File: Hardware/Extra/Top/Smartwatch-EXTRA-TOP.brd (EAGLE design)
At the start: 38 x 38 mm, 72 parts, among them U1 NRF52832_MODULE_MDBT42, U3 FT231XS, U4 PHOTOTRANSISTOR, U5 MCP9808-MSOP8

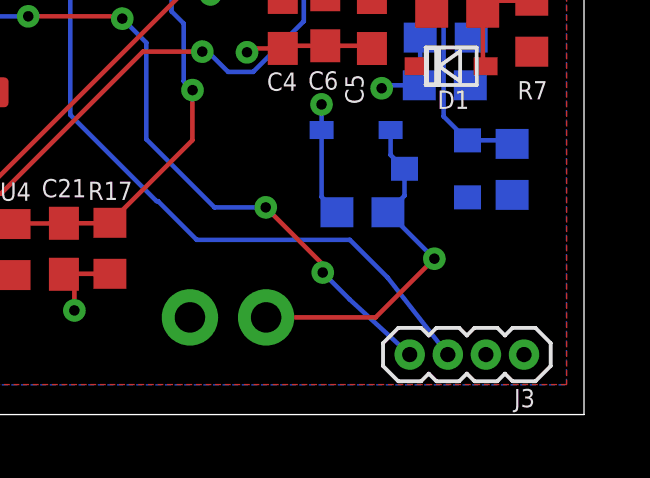
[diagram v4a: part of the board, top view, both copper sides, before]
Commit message: Encoder changed, BOMs updated
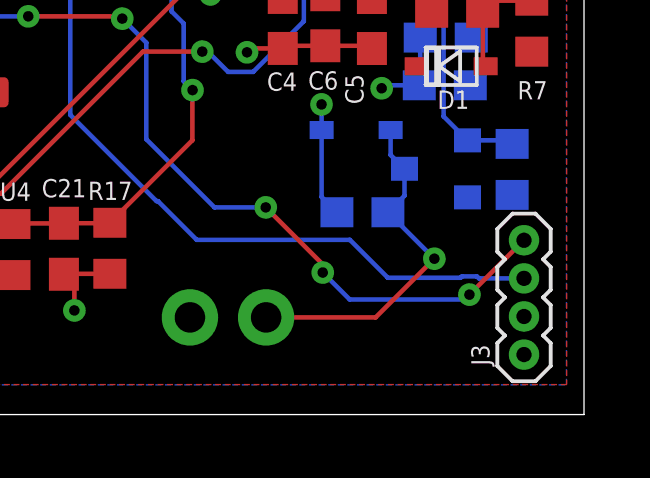
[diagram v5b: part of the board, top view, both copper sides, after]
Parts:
- C2: value 10u -> 10uF
- C21: value 2.2u -> 2.2uF
- C23: value 10p -> 10pF
- L1: value 10u -> 10uH
- turned J3 to 90 degrees
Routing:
- net SDA: track 63.8 -> 67.7 mm, vias 9 -> 10
- net SCL: track 61.5 -> 62.9 mm
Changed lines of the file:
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@@
 </layers>
 <board>
-<fusionsync huburn="a.YnVzaW5lc3M6cHVyZHVlMjIyNA" projecturn="a.YnVzaW5lc3M6cHVyZHVlMjIyNCMyMDIxMDMyNzM5NzIwMDMyNg" f3durn="urn:adsk.wipprod:dm.lineage:XFHoWaPkQBmQ3nj1vLUEBw" pcbguid="" lastpulledtime="" lastsyncedchangeguid="" latestrevisionid="3a5e7feb-a195-42dd-a08a-2611ee65cf8f" lastsyncedrevisionid="3a5e7feb-a195-42dd-a08a-2611ee65cf8f" lastboardhashguid="5192e39e-b93b-5078-4a78-5802325fcc51" lastpushedtime="2021-03-27T21:16:43Z" linktopcb3d="true"/>
+<fusionsync huburn="a.YnVzaW5lc3M6cHVyZHVlMjIyNA" projecturn="a.YnVzaW5lc3M6cHVyZHVlMjIyNCMyMDIxMDMyNzM5NzIwMDMyNg" f3durn="urn:adsk.wipprod:dm.lineage:XFHoWaPkQBmQ3nj1vLUEBw" pcbguid="" lastpulledtime="" lastsyncedchangeguid="" latestrevisionid="7c4fc147-7280-49f2-a8ff-9dc003aacbf2" lastsyncedrevisionid="7c4fc147-7280-49f2-a8ff-9dc003aacbf2" lastboardhashguid="22cbd7ec-4fab-d891-ac62-eccdf797752f" lastpushedtime="2021-03-27T21:42:09Z" linktopcb3d="true"/>
 <fusionteam huburn="a.YnVzaW5lc3M6cHVyZHVlMjIyNA" projecturn="a.YnVzaW5lc3M6cHVyZHVlMjIyNCNEMjAyMTAyMDYzODAwMDMxMjY" folderUrn="urn:adsk.wipprod:fs.folder:co.YdOB1KMQSXe9hTG6FhLD9w" urn="urn:adsk.wipprod:dm.lineage:W-tqdEdMRpy7A-WNC3jHJw"  versionUrn="urn:adsk.wipprod:fs.file:vf.W-tqdEdMRpy7A-WNC3jHJw?version=1" camFileUrn="" camFileVersionUrn="" lastpublishedchangeguid="9cd7a9d6-e81f-3132-e714-1a28a52f2c30"/>
 <plain>
@@
 <attribute name="VALUE" x="30.310865625" y="13.513784375" size="0.7112" layer="27" rot="R270"/>
 </element>
-<element name="C2" library="LinnesLab-Passives" package="C0805" override_package3d_urn="urn:adsk.eagle:package:27670968/2" override_package_urn="urn:adsk.eagle:footprint:27670970/1" value="10u" x="2.31901875" y="32.16148125" smashed="yes" rot="R90" grouprefs="MICROCONTROLLER">
+<element name="C2" library="LinnesLab-Passives" package="C0805" override_package3d_urn="urn:adsk.eagle:package:27670968/2" override_package_urn="urn:adsk.eagle:footprint:27670970/1" value="10uF" x="2.31901875" y="32.16148125" smashed="yes" rot="R90" grouprefs="MICROCONTROLLER">
 <attribute name="NAME" x="3.279140625" y="35.227259375" size="0.6096" layer="25" rot="R180"/>
 <attribute name="VALUE" x="4.22401875" y="30.89148125" size="0.7112" layer="27" rot="R90"/>
 </element>
-<element name="L1" library="LinnesLab-Passives" package="L0603" override_package3d_urn="urn:adsk.eagle:package:27669957/2" override_package_urn="urn:adsk.eagle:footprint:27669958/1" override_locally_modified="yes" value="10u" x="20.0353" y="25.997940625" smashed="yes" rot="R90" grouprefs="MICROCONTROLLER">
+<element name="L1" library="LinnesLab-Passives" package="L0603" override_package3d_urn="urn:adsk.eagle:package:27669957/2" override_package_urn="urn:adsk.eagle:footprint:27669958/1" override_locally_modified="yes" value="10uH" x="20.0353" y="25.997940625" smashed="yes" rot="R90" grouprefs="MICROCONTROLLER">
 <attribute name="NAME" x="20.907721875" y="26.149021875" size="0.6096" layer="25" rot="R270"/>
 <attribute name="VALUE" x="21.6863" y="25.362940625" size="0.7112" layer="27" rot="R90"/>
@@
 <attribute name="VALUE" x="32.697140625" y="18.93091875" size="0.7112" layer="27" rot="R270"/>
 </element>
-<element name="U1" library="LinnesLab-Microcontrollers" package="BLE_MODULE_RAYTAC_MDBT42" override_package3d_urn="urn:adsk.eagle:package:18593121/2" override_package_urn="urn:adsk.eagle:footprint:18593122/1" override_locally_modified="yes" value="NRF52832_MODULE_MDBT42" x="27.406" y="29.597" smashed="yes" grouprefs="MICROCONTROLLER">
+<element name="U1" library="LinnesLab-Microcontrollers" package="BLE_MODULE_RAYTAC_MDBT42" override_package3d_urn="urn:adsk.eagle:package:27726002/2" override_package_urn="urn:adsk.eagle:footprint:27726003/1" override_locally_modified="yes" value="NRF52832_MODULE_MDBT42" x="27.406" y="29.597" smashed="yes" grouprefs="MICROCONTROLLER">
 <attribute name="NAME" x="20.76961875" y="34.8617625" size="0.6096" layer="25" ratio="18"/>
 <attribute name="SPICEPREFIX" value="X" x="27.406" y="29.597" size="1.778" layer="27" display="off"/>
@@
 <attribute name="VALUE" x="24.100459375" y="4.906640625" size="1.27" layer="27" rot="R90"/>
 </element>
-<element name="C21" library="LinnesLab-Passives" package="C0603" override_package3d_urn="urn:adsk.eagle:package:27669811/2" override_package_urn="urn:adsk.eagle:footprint:27669812/1" value="2.2u" x="20.6638375" y="5.526403125" smashed="yes" rot="R270">
+<element name="C21" library="LinnesLab-Passives" package="C0603" override_package3d_urn="urn:adsk.eagle:package:27669811/2" override_package_urn="urn:adsk.eagle:footprint:27669812/1" value="2.2uF" x="20.6638375" y="5.526403125" smashed="yes" rot="R270">
 <attribute name="NAME" x="21.40648125" y="7.850203125" size="0.6096" layer="25" rot="R180"/>
 <attribute name="VALUE" x="18.7588375" y="6.161403125" size="1.27" layer="27" rot="R270"/>
 </element>
-<element name="J3" library="LinnesLab-Connectors" package="1X04_1.27MM" override_package3d_urn="urn:adsk.eagle:package:27725590/2" override_package_urn="urn:adsk.eagle:footprint:27725591/1" value="" x="36" y="2" smashed="yes" rot="R180">
-<attribute name="NAME" x="36.365759375" y="0.851921875" size="0.6096" layer="25" font="vector" ratio="20" rot="R180"/>
-<attribute name="VALUE" x="36.381" y="3.651" size="0.6096" layer="27" font="vector" ratio="20" rot="R180"/>
+<element name="J3" library="LinnesLab-Connectors" package="1X04_1.27MM" override_package3d_urn="urn:adsk.eagle:package:27725590/2" override_package_urn="urn:adsk.eagle:footprint:27725591/1" value="" x="36" y="2" smashed="yes" rot="R90">
+<attribute name="NAME" x="34.851921875" y="1.634240625" size="0.6096" layer="25" font="vector" ratio="20" rot="R90"/>
+<attribute name="VALUE" x="37.651" y="1.619" size="0.6096" layer="27" font="vector" ratio="20" rot="R90"/>
 </element>
 <element name="C22" library="LinnesLab-Passives" package="C0603" override_package3d_urn="urn:adsk.eagle:package:27669815/2" override_package_urn="urn:adsk.eagle:footprint:27669816/1" value="100n" x="13.0403875" y="26.00068125" smashed="yes" rot="R90">
@@
 <attribute name="VALUE" x="31.673959375" y="7.8189875" size="0.635" layer="28" rot="MR0"/>
 </element>
-<element name="C23" library="LinnesLab-Passives" package="C0603" override_package3d_urn="urn:adsk.eagle:package:27669817/2" override_package_urn="urn:adsk.eagle:footprint:27669818/1" value="10p" x="30.614775" y="6.743328125" smashed="yes" rot="MR0">
+<element name="C23" library="LinnesLab-Passives" package="C0603" override_package3d_urn="urn:adsk.eagle:package:27669817/2" override_package_urn="urn:adsk.eagle:footprint:27669818/1" value="10pF" x="30.614775" y="6.743328125" smashed="yes" rot="MR0">
 <attribute name="NAME" x="31.033875" y="7.58406875" size="0.6096" layer="26" rot="MR0"/>
 <attribute name="VALUE" x="31.249775" y="4.838328125" size="1.27" layer="28" rot="MR0"/>
@@
 <attribute name="VALUE" x="32.755684375" y="14.470746875" size="1.27" layer="28" rot="MR180"/>
 </element>
-<element name="J4" library="LinnesLab-Connectors" package="1X03_1.27MM" override_package3d_urn="urn:adsk.eagle:package:27725632/2" override_package_urn="urn:adsk.eagle:footprint:27725633/1" value="" x="13.89" y="33" smashed="yes">
+<element name="J4" library="LinnesLab-Connectors" package="1X03_1.27MM" override_package3d_urn="urn:adsk.eagle:package:27725632/3" override_package_urn="urn:adsk.eagle:footprint:27725633/1" value="" x="13.89" y="33" smashed="yes">
 <attribute name="NAME" x="13.509" y="34.016" size="0.6096" layer="25" font="vector" ratio="20"/>
 <attribute name="VALUE" x="13.509" y="31.349" size="0.6096" layer="27" font="vector" ratio="20"/>
@@
 <via x="29.29128125" y="4.734559375" extent="1-16" drill="0.35"/>
 <wire x1="29.29128125" y1="4.734559375" x2="30.19" y2="3.835840625" width="0.1524" layer="16"/>
-<wire x1="30.19" y1="3.835840625" x2="32.19" y2="2" width="0.1524" layer="16"/>
+<wire x1="30.19" y1="3.835840625" x2="34.0186625" y2="3.835840625" width="0.1524" layer="16"/>
+<wire x1="34.0186625" y1="3.835840625" x2="34.18078125" y2="3.997959375" width="0.1524" layer="16"/>
+<via x="34.18078125" y="3.997959375" extent="1-16" drill="0.35"/>
+<wire x1="34.18078125" y1="3.997959375" x2="35.992821875" y2="5.81" width="0.1524" layer="1"/>
+<wire x1="35.992821875" y1="5.81" x2="36" y2="5.81" width="0.1524" layer="1"/>
 </signal>
 <signal name="SCL">
@@
 <wire x1="25.09001875" y1="5.82421875" x2="30.195521875" y2="5.82421875" width="0.1524" layer="16"/>
 <wire x1="30.195521875" y1="5.82421875" x2="31.46" y2="4.559740625" width="0.1524" layer="16"/>
-<wire x1="31.46" y1="4.559740625" x2="33.46" y2="2" width="0.1524" layer="16"/>
 <wire x1="23.800975" y1="7.1132625" x2="25.09001875" y2="5.82421875" width="0.1524" layer="16"/>
+<wire x1="33.92943125" y1="4.6047625" x2="34.43213125" y2="4.6047625" width="0.1524" layer="16"/>
+<wire x1="34.43213125" y1="4.6047625" x2="34.49689375" y2="4.54" width="0.1524" layer="16"/>
+<wire x1="34.49689375" y1="4.54" x2="36" y2="4.54" width="0.1524" layer="16"/>
+<wire x1="31.46" y1="4.559740625" x2="33.884409375" y2="4.559740625" width="0.1524" layer="16"/>
+<wire x1="33.884409375" y1="4.559740625" x2="33.92943125" y2="4.6047625" width="0.1524" layer="16"/>
 </signal>
 <signal name="SCK">

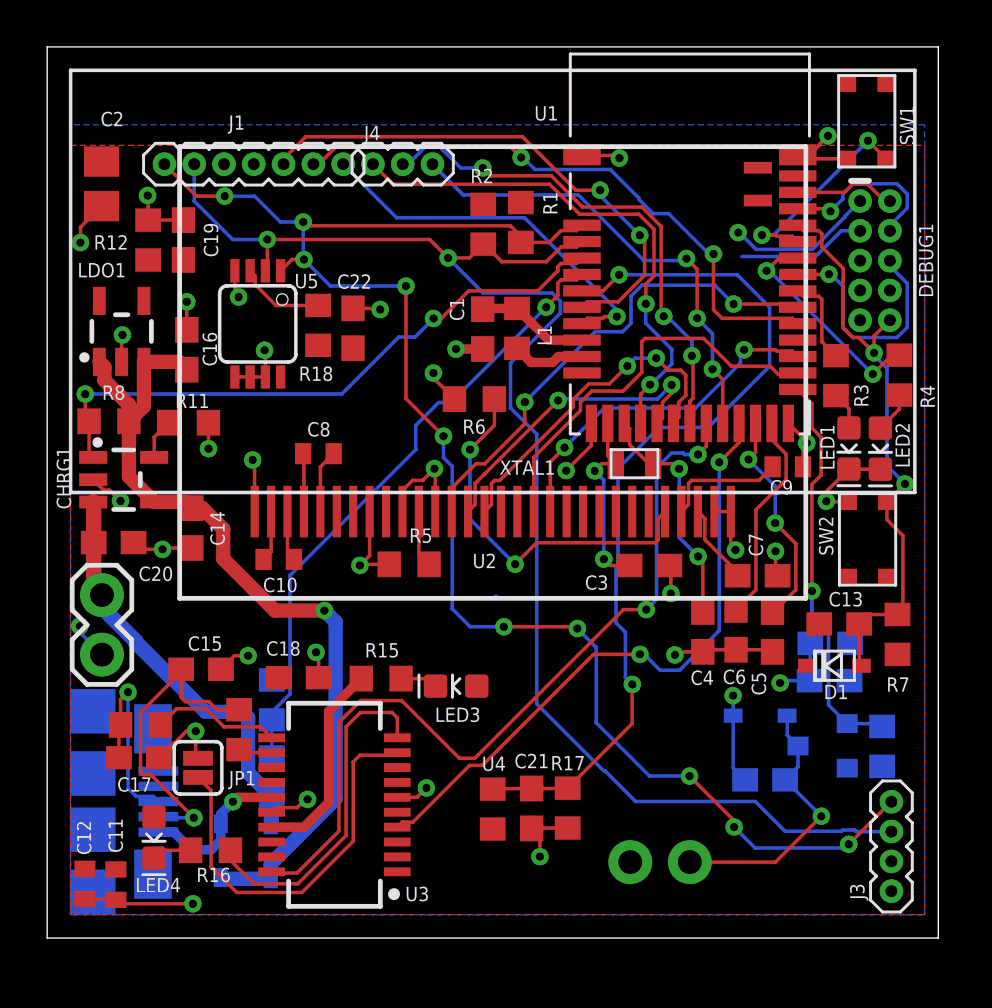
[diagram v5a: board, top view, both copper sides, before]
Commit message: Removed GPS, rearranged some other components
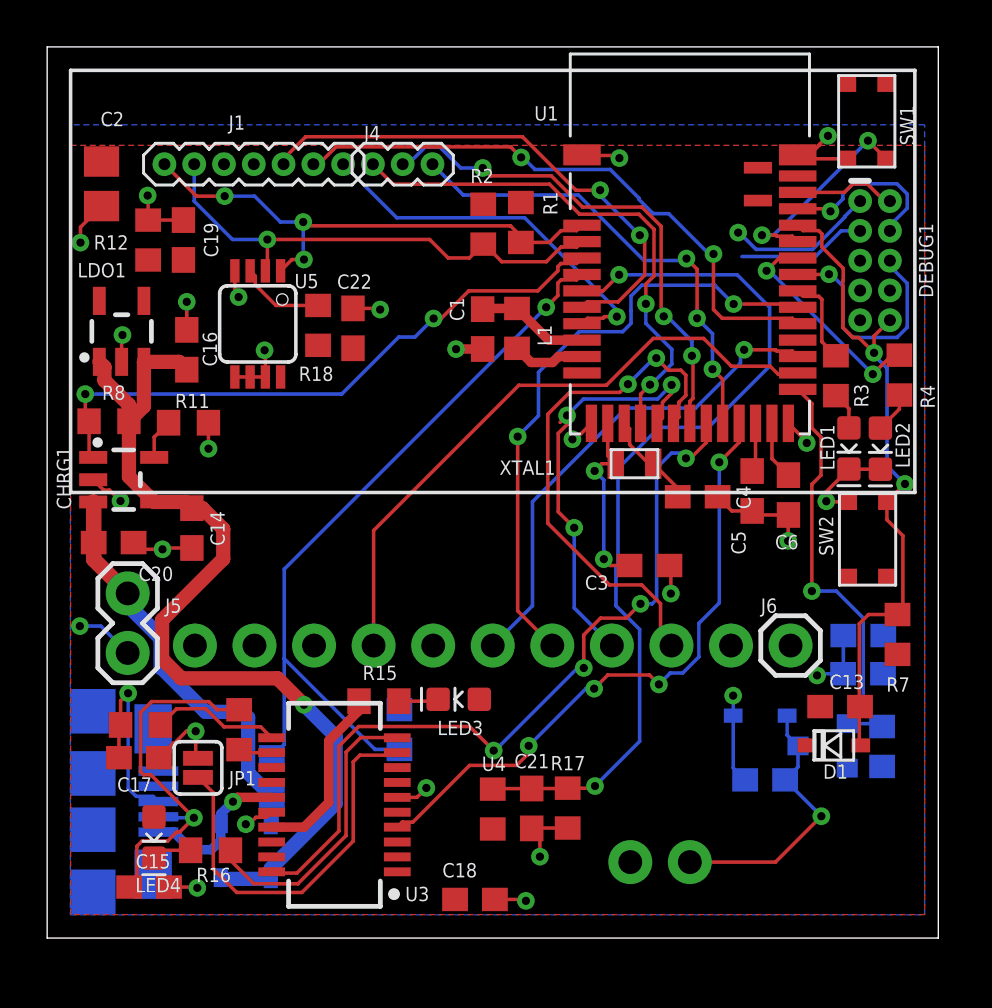
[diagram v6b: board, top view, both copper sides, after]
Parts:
- removed C10, C11, C12, C8, C9: 2.2uF, LinnesLab-Passives:C0402
- removed C7: 10uF, LinnesLab-Passives:C0603
- removed J3: (no value), LinnesLab-Connectors:1X04_1.27MM
- removed R5: 10k, LinnesLab-Passives:R0603
- removed R6: 390k, LinnesLab-Passives:R0603
- removed U2: (no value), LinnesLab-Displays:UG-2864HSWEG01_0.96IN_NO-WRAPAROUND
- added J5: (no value), LinnesLab-Connectors:1X10_NO_SILK
- added J6: (no value), LinnesLab-Connectors:1X01
- moved C18 12.1 mm to (18.2, 1.65)
- moved C15 9.55 mm to (4.34, 2.17)
- moved C6 6.17 mm to (31.6, 18.9)
- moved C5 6.07 mm to (30.1, 19.1)
- moved C4 5.77 mm to (27.7, 18.8), turned to 0 degrees
- moved R14 5.59 mm to (15.0, 8.89)
- moved C13 3.52 mm to (33.8, 9.87)
- moved D1 3.40 mm to (33.5, 8.21)
- moved C24 1.46 mm to (34.8, 11.3)
- moved C25 1.45 mm to (34.8, 12.9)
- moved J2 1.10 mm to (3.43, 12.2)
- moved R15 0.97 mm to (14.1, 10.1)
- moved LED3 0.57 mm to (17.5, 10.2)
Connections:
- removed net N$1: R5.2, U2.11
- removed net N$13: C7.2, U2.28
- removed net N$15: C9.2, U2.27
- removed net N$2: R6.1, U2.26
- removed net N$3: C10.2, U2.2
- removed net N$5: C10.1, U2.3
- removed net N$7: C8.2, U2.4
- removed net N$8: C8.1, U2.5
- new net 3: J5.5
- new net 3.3VO: J5.2
- new net LIT: J6.1
- new net SDCS: J5.10
- net 3.3V: now also J5.1; no longer C11.2, C12.2, J3.2, U2.6, U2.9
- net D16/CS.OLED: now also J5.7; no longer U2.13
- net D3/RESET.OLED: now also J5.8; no longer U2.14
- net D4/DC.OLED: now also J5.9; no longer U2.15
- net GND: now also J5.3; no longer C11.1, C12.1, C7.1, C9.1, J3.1, R5.1, R6.2, U2.1, U2.10, U2.12, U2.29, U2.30, U2.8
- net MOSI: now also J5.6; no longer U2.19
- net SCK: now also J5.4; no longer U2.18
- net SCL: no longer J3.3
- net SDA: no longer J3.4
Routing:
- net SDA: track 67.7 -> 22.5 mm, vias 10 -> 3
- net SCL: track 62.9 -> 21.4 mm, vias 2 -> 1
- net GND: track 77.1 -> 55.3 mm, vias 32 -> 25
- net N$2: track 16.1 -> 0.00 mm, vias 2 -> 0
- net SCK: track 17.3 -> 27.0 mm
- net D4/DC.OLED: track 14.6 -> 22.3 mm
- net P0.09/NFC1: track 9.44 -> 2.09 mm, vias 2 -> 0
- net P0.10/NFC2: track 9.09 -> 2.50 mm
- net A4/BATT: track 26.7 -> 33.0 mm
- net MOSI: track 15.0 -> 21.2 mm, vias 2 -> 1
- net N$6: track 10.1 -> 4.19 mm, vias 2 -> 0
- net D16/CS.OLED: track 21.0 -> 26.3 mm
- net N$15: track 5.20 -> 0.00 mm
- net D3/RESET.OLED: track 13.3 -> 18.2 mm, vias 2 -> 3
- net N$13: track 3.44 -> 0.00 mm
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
